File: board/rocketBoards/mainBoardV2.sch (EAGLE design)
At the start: 60 parts, among them J1 47346-0001

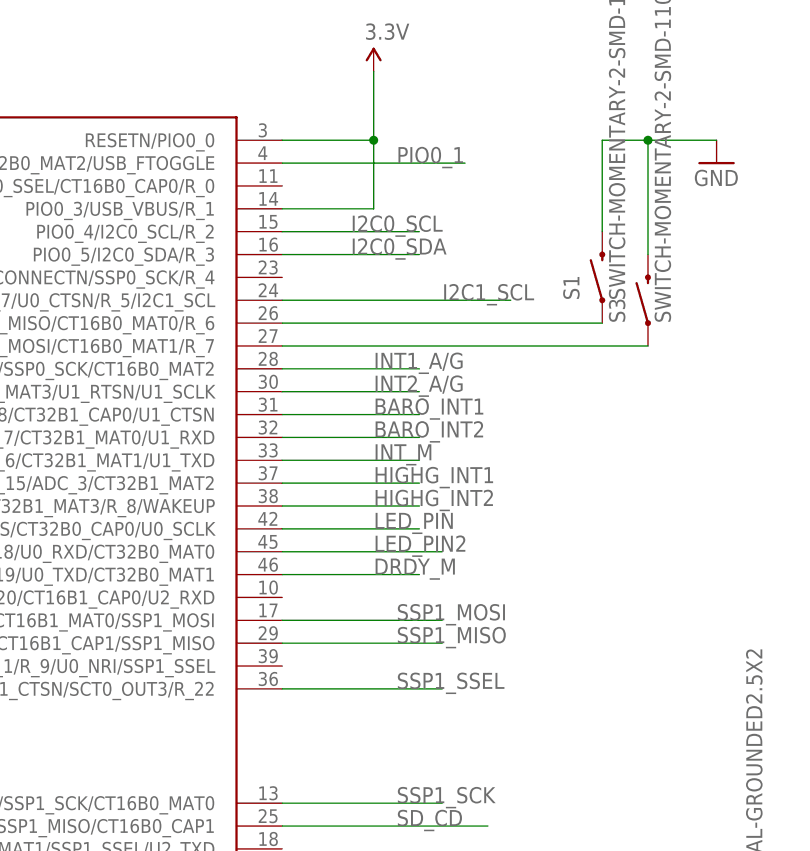
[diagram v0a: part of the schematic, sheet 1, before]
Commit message: added ThinMan basic board
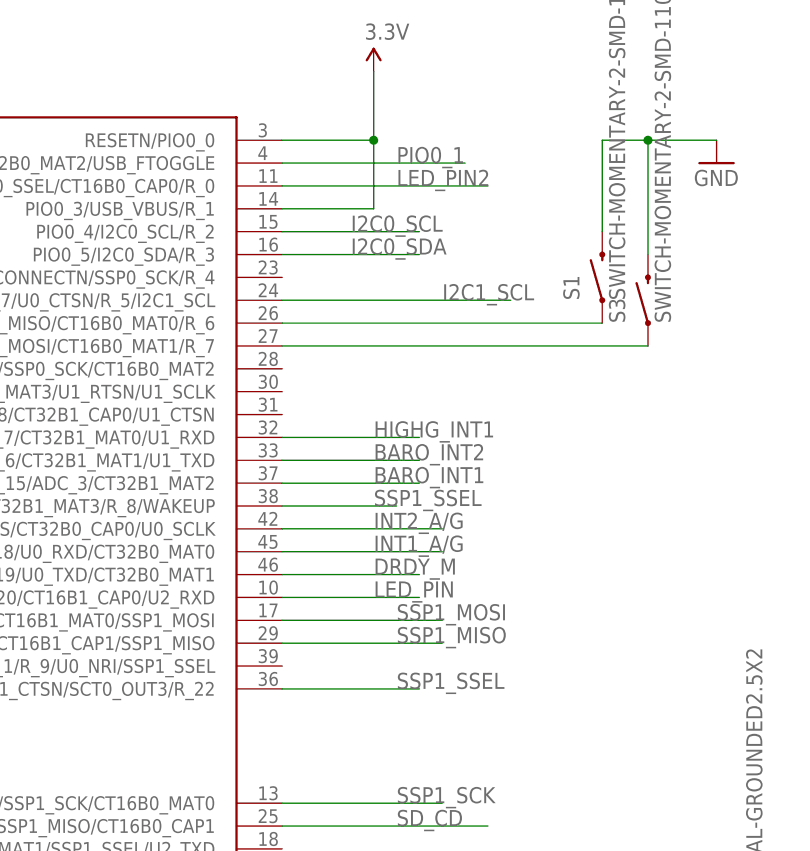
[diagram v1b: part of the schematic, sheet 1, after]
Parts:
- removed JP1: M02JST-PTH-2, SparkFun-Connectors:M02JST-PTH-2
- added JP3: M02JST-PTH-2, SparkFun-Connectors:M02JST-PTH-2
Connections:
- net BARO_INT1: now also U1.SWDIO/PIO0_15/ADC_3/CT32B1_MAT2; no longer U1.TMS/PIO0_12/ADC_8/CT32B1_CAP0/U1_CTSN
- net BARO_INT2: now also U1.TRSTN/PIO0_14/ADC_6/CT32B1_MAT1/U1_TXD; no longer U1.TDO/PIO0_13/ADC_7/CT32B1_MAT0/U1_RXD
- net HIGHG_INT1: now also U1.TDO/PIO0_13/ADC_7/CT32B1_MAT0/U1_RXD; no longer U1.SWDIO/PIO0_15/ADC_3/CT32B1_MAT2
- net HIGHG_INT2: now also U1.PIO1_13/U1_CTSN/SCT0_OUT3/R_22; no longer U1.PIO0_16/ADC_2/CT32B1_MAT3/R_8/WAKEUP
- net I2C0_SCL: now also JP3.1
- net I2C0_SDA: now also JP3.2
- net I2C1_SCL: no longer JP1.1
- net I2C1_SDA: no longer JP1.2
- net INT1_A/G: now also U1.PIO0_18/U0_RXD/CT32B0_MAT0; no longer U1.SWCLK/PIO0_10/SSP0_SCK/CT16B0_MAT2
- net INT2_A/G: now also U1.PIO0_17/U0_RTS/CT32B0_CAP0/U0_SCLK; no longer U1.TDI/PIO0_11/ADC_9/CT32B0_MAT3/U1_RTSN/U1_SCLK
- net INT_M: no longer U1.TRSTN/PIO0_14/ADC_6/CT32B1_MAT1/U1_TXD
- net LED_PIN: now also U1.PIO0_20/CT16B1_CAP0/U2_RXD; no longer U1.PIO0_17/U0_RTS/CT32B0_CAP0/U0_SCLK
- net LED_PIN2: now also U1.PIO0_2/SSP0_SSEL/CT16B0_CAP0/R_0; no longer U1.PIO0_18/U0_RXD/CT32B0_MAT0
- net SSP1_SSEL: now also U1.PIO0_16/ADC_2/CT32B1_MAT3/R_8/WAKEUP; no longer U1.PIO1_13/U1_CTSN/SCT0_OUT3/R_22
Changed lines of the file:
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@@
 </part>
 <part name="SUPPLY16" library="SparkFun-Aesthetics" deviceset="3.3V" device=""/>
-<part name="JP1" library="SparkFun-Connectors" deviceset="M02" device="JST-PTH-2">
-<attribute name="MF" value=""/>
-<attribute name="MPN" value=""/>
-<attribute name="OC_NEWARK" value="unknown"/>
-</part>
 <part name="LED1" library="adafruit" deviceset="LED" device="CHIPLED_0603">
 <attribute name="MF" value=""/>
@@
 <part name="J1" library="ELL-i-Connectors" deviceset="MICRO-USB" device="" value="47346-0001"/>
 <part name="GND11" library="SparkFun-Aesthetics" deviceset="GND" device=""/>
+<part name="JP3" library="SparkFun-Connectors" deviceset="M02" device="JST-PTH-2">
+<attribute name="MF" value=""/>
+<attribute name="MPN" value=""/>
+<attribute name="OC_NEWARK" value="unknown"/>
+</part>
 </parts>
 <sheets>
@@
 <net name="SSP1_SSEL" class="0">
 <segment>
-<pinref part="U1" gate="G$1" pin="PIO1_13/U1_CTSN/SCT0_OUT3/R_22"/>
-<wire x1="106.68" y1="106.68" x2="124.46" y2="106.68" width="0.1524" layer="91"/>
+<pinref part="U1" gate="G$1" pin="PIO0_16/ADC_2/CT32B1_MAT3/R_8/WAKEUP"/>
+<wire x1="106.68" y1="127" x2="119.38" y2="127" width="0.1524" layer="91"/>
 <label x="119.38" y="106.68" size="1.778" layer="95"/>
+<label x="116.84" y="127" size="1.778" layer="95"/>
 </segment>
 </net>
@@
 <net name="INT1_A/G" class="0">
 <segment>
-<pinref part="U1" gate="G$1" pin="SWCLK/PIO0_10/SSP0_SCK/CT16B0_MAT2"/>
-<wire x1="106.68" y1="142.24" x2="121.92" y2="142.24" width="0.1524" layer="91"/>
-<label x="116.84" y="142.24" size="1.778" layer="95"/>
+<pinref part="U1" gate="G$1" pin="PIO0_18/U0_RXD/CT32B0_MAT0"/>
+<wire x1="106.68" y1="121.92" x2="124.46" y2="121.92" width="0.1524" layer="91"/>
+<label x="116.84" y="121.92" size="1.778" layer="95"/>
 </segment>
 </net>
 <net name="INT2_A/G" class="0">
 <segment>
-<pinref part="U1" gate="G$1" pin="TDI/PIO0_11/ADC_9/CT32B0_MAT3/U1_RTSN/U1_SCLK"/>
-<wire x1="106.68" y1="139.7" x2="121.92" y2="139.7" width="0.1524" layer="91"/>
-<label x="116.84" y="139.7" size="1.778" layer="95"/>
+<pinref part="U1" gate="G$1" pin="PIO0_17/U0_RTS/CT32B0_CAP0/U0_SCLK"/>
+<wire x1="106.68" y1="124.46" x2="124.46" y2="124.46" width="0.1524" layer="91"/>
+<label x="116.84" y="124.46" size="1.778" layer="95"/>
 </segment>
 </net>
 <net name="BARO_INT1" class="0">
 <segment>
-<pinref part="U1" gate="G$1" pin="TMS/PIO0_12/ADC_8/CT32B1_CAP0/U1_CTSN"/>
-<wire x1="106.68" y1="137.16" x2="121.92" y2="137.16" width="0.1524" layer="91"/>
-<label x="116.84" y="137.16" size="1.778" layer="95"/>
+<pinref part="U1" gate="G$1" pin="SWDIO/PIO0_15/ADC_3/CT32B1_MAT2"/>
+<wire x1="106.68" y1="129.54" x2="121.92" y2="129.54" width="0.1524" layer="91"/>
+<label x="116.84" y="129.54" size="1.778" layer="95"/>
 </segment>
 </net>
 <net name="BARO_INT2" class="0">
+<segment>
+<pinref part="U1" gate="G$1" pin="TRSTN/PIO0_14/ADC_6/CT32B1_MAT1/U1_TXD"/>
+<wire x1="106.68" y1="132.08" x2="121.92" y2="132.08" width="0.1524" layer="91"/>
+<label x="116.84" y="132.08" size="1.778" layer="95"/>
+</segment>
+</net>
+<net name="HIGHG_INT1" class="0">
 <segment>
 <pinref part="U1" gate="G$1" pin="TDO/PIO0_13/ADC_7/CT32B1_MAT0/U1_RXD"/>
@@
 </segment>
 </net>
-<net name="INT_M" class="0">
-<segment>
-<pinref part="U1" gate="G$1" pin="TRSTN/PIO0_14/ADC_6/CT32B1_MAT1/U1_TXD"/>
-<wire x1="106.68" y1="132.08" x2="121.92" y2="132.08" width="0.1524" layer="91"/>
-<label x="116.84" y="132.08" size="1.778" layer="95"/>
-</segment>
-</net>
-<net name="HIGHG_INT1" class="0">
-<segment>
-<pinref part="U1" gate="G$1" pin="SWDIO/PIO0_15/ADC_3/CT32B1_MAT2"/>
-<wire x1="106.68" y1="129.54" x2="121.92" y2="129.54" width="0.1524" layer="91"/>
-<label x="116.84" y="129.54" size="1.778" layer="95"/>
-</segment>
-</net>
 <net name="HIGHG_INT2" class="0">
 <segment>
-<pinref part="U1" gate="G$1" pin="PIO0_16/ADC_2/CT32B1_MAT3/R_8/WAKEUP"/>
-<wire x1="106.68" y1="127" x2="121.92" y2="127" width="0.1524" layer="91"/>
-<label x="116.84" y="127" size="1.778" layer="95"/>
+<pinref part="U1" gate="G$1" pin="PIO1_13/U1_CTSN/SCT0_OUT3/R_22"/>
+<wire x1="106.68" y1="106.68" x2="121.92" y2="106.68" width="0.1524" layer="91"/>
 </segment>
 </net>
@@
 <net name="LED_PIN" class="0">
 <segment>
-<pinref part="U1" gate="G$1" pin="PIO0_17/U0_RTS/CT32B0_CAP0/U0_SCLK"/>
-<wire x1="106.68" y1="124.46" x2="121.92" y2="124.46" width="0.1524" layer="91"/>
-<label x="116.84" y="124.46" size="1.778" layer="95"/>
+<pinref part="U1" gate="G$1" pin="PIO0_20/CT16B1_CAP0/U2_RXD"/>
+<wire x1="106.68" y1="116.84" x2="121.92" y2="116.84" width="0.1524" layer="91"/>
+<label x="116.84" y="116.84" size="1.778" layer="95"/>
 </segment>
 </net>
@@
 <net name="LED_PIN2" class="0">
 <segment>
-<pinref part="U1" gate="G$1" pin="PIO0_18/U0_RXD/CT32B0_MAT0"/>
-<wire x1="106.68" y1="121.92" x2="124.46" y2="121.92" width="0.1524" layer="91"/>
-<label x="116.84" y="121.92" size="1.778" layer="95"/>
+<pinref part="U1" gate="G$1" pin="PIO0_2/SSP0_SSEL/CT16B0_CAP0/R_0"/>
+<wire x1="106.68" y1="162.56" x2="129.54" y2="162.56" width="0.1524" layer="91"/>
+<label x="119.38" y="162.56" size="1.778" layer="95"/>
 </segment>
 </net>
@@
 <attribute name="MPN" x="200.66" y="38.1" size="1.778" layer="96" display="off"/>
 </instance>
-<instance part="JP1" gate="G$1" x="45.72" y="53.34">
-<attribute name="OC_NEWARK" x="45.72" y="53.34" size="1.778" layer="96" display="off"/>
-<attribute name="MF" x="45.72" y="53.34" size="1.778" layer="96" display="off"/>
-<attribute name="MPN" x="45.72" y="53.34" size="1.778" layer="96" display="off"/>
-</instance>
 <instance part="C20" gate="G$1" x="200.66" y="43.18" rot="R90">
 <attribute name="OC_NEWARK" x="200.66" y="43.18" size="1.778" layer="96" display="off"/>
@@
 <instance part="C16" gate="G$1" x="223.52" y="48.26"/>
 <instance part="R6" gate="G$1" x="195.58" y="33.02"/>
+<instance part="JP3" gate="G$1" x="48.26" y="73.66">
+<attribute name="OC_NEWARK" x="48.26" y="73.66" size="1.778" layer="96" display="off"/>
+<attribute name="MF" x="48.26" y="73.66" size="1.778" layer="96" display="off"/>
+<attribute name="MPN" x="48.26" y="73.66" size="1.778" layer="96" display="off"/>
+</instance>
 </instances>
 <busses>
@@
 <label x="55.88" y="71.12" size="1.778" layer="95"/>
 <pinref part="R3" gate="G$1" pin="2"/>
+<pinref part="JP3" gate="G$1" pin="1"/>
+<wire x1="55.88" y1="71.12" x2="55.88" y2="73.66" width="0.1524" layer="91"/>
 </segment>
 <segment>
@@
 <label x="55.88" y="76.2" size="1.778" layer="95"/>
 <pinref part="R2" gate="G$1" pin="2"/>
+<pinref part="JP3" gate="G$1" pin="2"/>
 </segment>
 <segment>
@@
 <label x="55.88" y="55.88" size="1.778" layer="95"/>
 <pinref part="R1" gate="G$1" pin="2"/>
-<pinref part="JP1" gate="G$1" pin="2"/>
 </segment>
 </net>
@@
 <label x="55.88" y="50.8" size="1.778" layer="95"/>
 <pinref part="R4" gate="G$1" pin="2"/>
-<pinref part="JP1" gate="G$1" pin="1"/>
 <wire x1="53.34" y1="50.8" x2="53.34" y2="53.34" width="0.1524" layer="91"/>
 </segment>
